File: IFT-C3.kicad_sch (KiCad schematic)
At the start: 47 parts, among them IC1 DIO5508XS8, J1 Conn_01x04_Socket, J2 Conn_01x10_Pin, J3 USB4085-GF-A_REVB, J4 Conn_01x10_Pin, J5 SJ-3523-SMT-TR, J6 Conn_01x02_Pin, J7 Conn_01x02, Q12 Q_Photo_NPN, Q2 Q_NMOS_GSD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

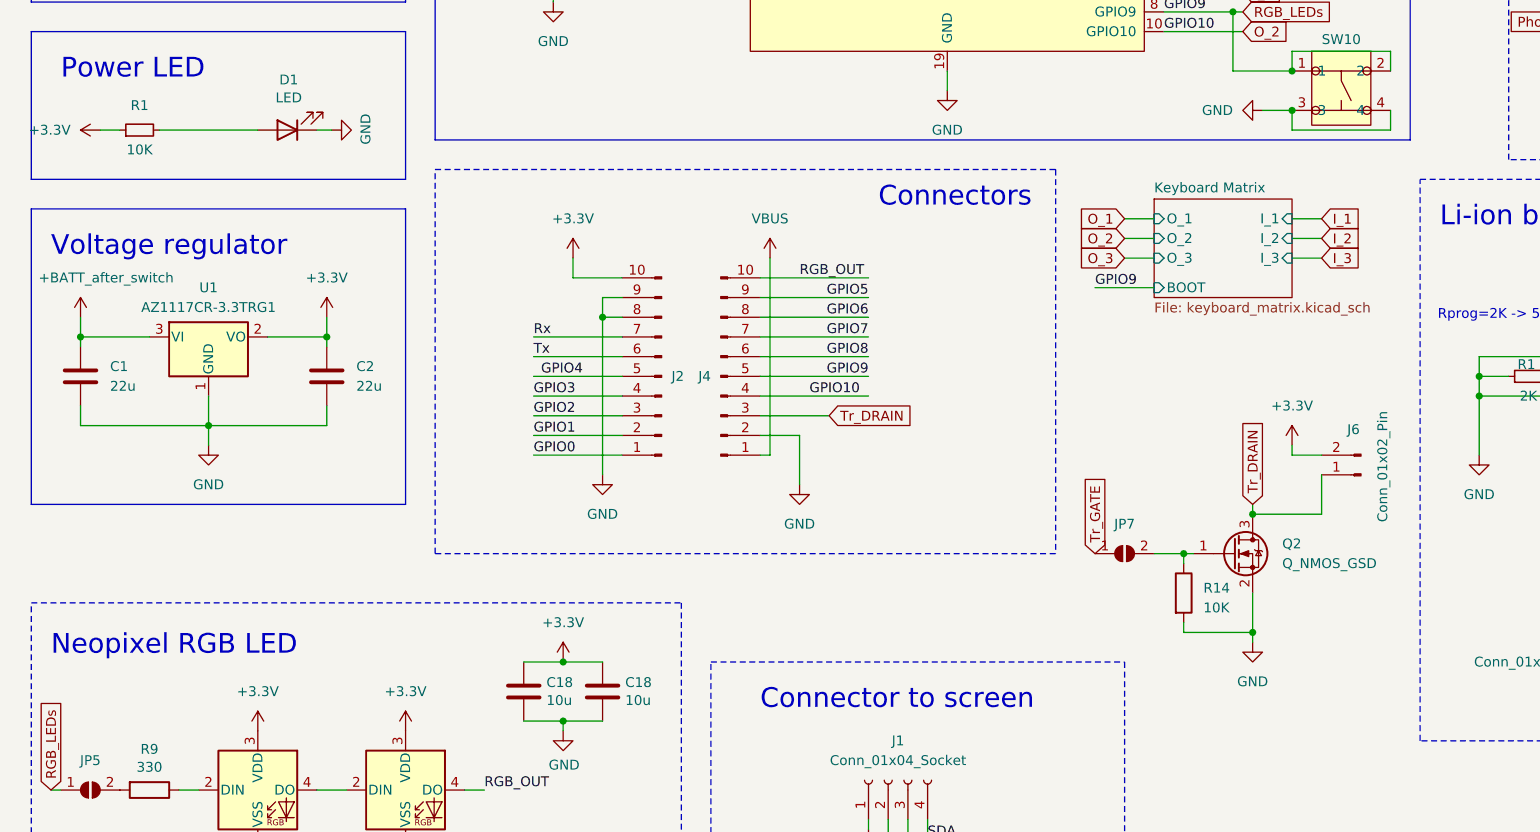
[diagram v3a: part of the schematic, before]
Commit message: Buttons fixed, boot buuton added, footprint of the switch should be easier to solder by hand
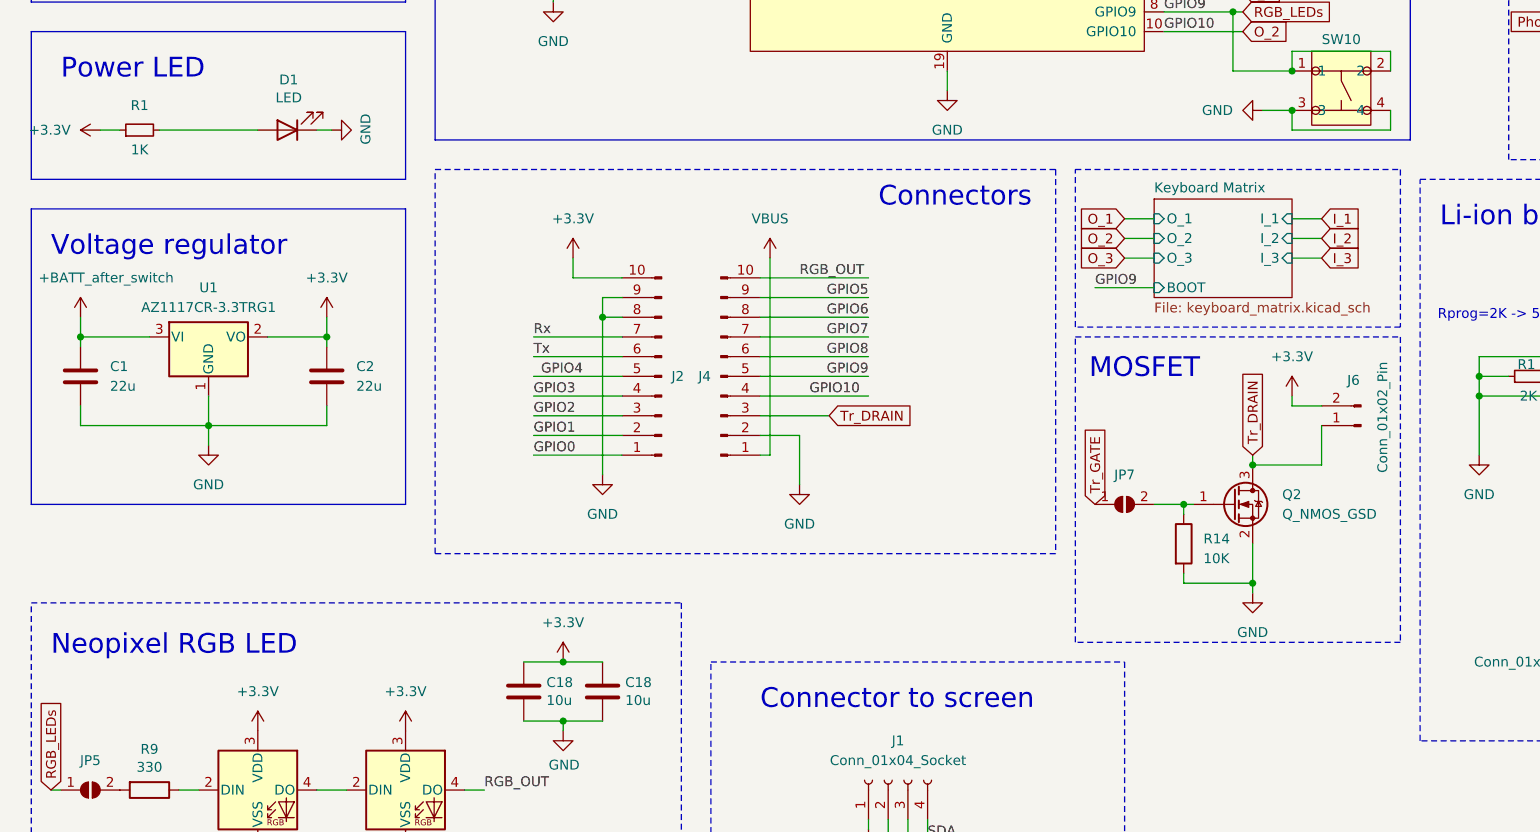
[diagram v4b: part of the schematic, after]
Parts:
- J2, J4: footprint Connector_PinHeader_2.54mm:PinHeader_1x10_P2.54mm_Horizontal -> Connector_PinHeader_2.54mm:PinHeader_1x10_P2.54mm_Vertical
- R1: value 10K -> 1K
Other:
- note added: "MOSFET"
- moved on the sheet: J6, JP7, Q2, R14
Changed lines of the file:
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@@
 	)
 	(junction
-		(at 173.99 149.86)
+		(at 173.99 143.51)
 		(diameter 0)
 		(color 0 0 0 0)
@@
 	)
 	(junction
-		(at 173.99 134.62)
+		(at 173.99 128.27)
 		(diameter 0)
 		(color 0 0 0 0)
@@
 	)
 	(junction
-		(at 165.1 139.7)
+		(at 165.1 133.35)
 		(diameter 0)
 		(color 0 0 0 0)
@@
 	(wire
 		(pts
-			(xy 165.1 148.59) (xy 165.1 149.86)
+			(xy 165.1 142.24) (xy 165.1 143.51)
 		)
 		(stroke
@@
 	(wire
 		(pts
-			(xy 166.37 139.7) (xy 165.1 139.7)
+			(xy 166.37 133.35) (xy 165.1 133.35)
 		)
 		(stroke
@@
 	(wire
 		(pts
-			(xy 165.1 149.86) (xy 173.99 149.86)
+			(xy 165.1 143.51) (xy 173.99 143.51)
 		)
 		(stroke
@@
 	(wire
 		(pts
-			(xy 182.88 129.54) (xy 182.88 134.62)
+			(xy 182.88 123.19) (xy 182.88 128.27)
 		)
 		(stroke
@@
 	(wire
 		(pts
-			(xy 182.88 134.62) (xy 173.99 134.62)
+			(xy 182.88 128.27) (xy 173.99 128.27)
 		)
 		(stroke
@@
 	(wire
 		(pts
-			(xy 173.99 149.86) (xy 173.99 151.13)
+			(xy 173.99 143.51) (xy 173.99 144.78)
 		)
 		(stroke
@@
 	(wire
 		(pts
-			(xy 173.99 144.78) (xy 173.99 149.86)
+			(xy 173.99 138.43) (xy 173.99 143.51)
 		)
 		(stroke
@@
 	(wire
 		(pts
-			(xy 182.88 127) (xy 179.07 127)
+			(xy 182.88 120.65) (xy 179.07 120.65)
 		)
 		(stroke
@@
 	(wire
 		(pts
-			(xy 179.07 127) (xy 179.07 125.73)
+			(xy 179.07 120.65) (xy 179.07 119.38)
 		)
 		(stroke
@@
 	(wire
 		(pts
-			(xy 173.99 133.35) (xy 173.99 134.62)
+			(xy 173.99 127) (xy 173.99 128.27)
 		)
 		(stroke
@@
 	(wire
 		(pts
-			(xy 165.1 139.7) (xy 165.1 140.97)
+			(xy 165.1 133.35) (xy 165.1 134.62)
 		)
 		(stroke
@@
 	(wire
 		(pts
-			(xy 161.29 139.7) (xy 165.1 139.7)
+			(xy 161.29 133.35) (xy 165.1 133.35)
 		)
 		(stroke
@@
 	)
 	(rectangle
+		(start 151.13 90.17)
+		(end 193.04 110.49)
+		(stroke
+			(width 0)
+			(type dash)
+		)
+		(fill
+			(type none)
+		)
+	)
+	(rectangle
 		(start 195.58 91.44)
 		(end 281.94 163.83)
@@
 	)
 	(rectangle
+		(start 151.13 111.76)
+		(end 193.04 151.13)
+		(stroke
+			(width 0)
+			(type dash)
+		)
+		(fill
+			(type none)
+		)
+	)
+	(rectangle
 		(start 250.19 52.07)
 		(end 281.94 88.9)
@@
 		)
 	)
+	(text "MOSFET"
+		(exclude_from_sim no)
+		(at 152.908 117.348 0)
+		(effects
+			(font
+				(size 2.54 2.54)
+			)
+			(justify left bottom)
+		)
+	)
 	(text "Audio output"
 		(exclude_from_sim no)
@@
 	(global_label "Tr_GATE"
 		(shape input)
-		(at 153.67 139.7 90)
+		(at 153.67 133.35 90)
 		(fields_autoplaced yes)
 		(effects
@@
 		)
 		(property "Intersheetrefs" "${INTERSHEET_REFS}"
-			(at 153.67 130.1724 90)
+			(at 153.67 123.8224 90)
 			(effects
 				(font
@@
 	(global_label "Tr_DRAIN"
 		(shape input)
-		(at 173.99 133.35 90)
+		(at 173.99 127 90)
 		(fields_autoplaced yes)
 		(effects
@@
 		)
 		(property "Intersheetrefs" "${INTERSHEET_REFS}"
-			(at 173.99 122.7337 90)
+			(at 173.99 116.3837 90)
 			(effects
 				(font
@@
 	(symbol
 		(lib_id "Device:Q_NMOS_GSD")
-		(at 171.45 139.7 0)
+		(at 171.45 133.35 0)
 		(unit 1)
 		(exclude_from_sim no)
@@
 		(fields_autoplaced yes)
 		(property "Reference" "Q2"
-			(at 177.8 138.43 0)
+			(at 177.8 132.08 0)
 			(effects
 				(font
@@
 		)
 		(property "Value" "Q_NMOS_GSD"
-			(at 177.8 140.97 0)
+			(at 177.8 134.62 0)
 			(effects
 				(font
@@
 		)
 		(property "Footprint" "Package_TO_SOT_SMD:SOT-23-3"
-			(at 176.53 137.16 0)
+			(at 176.53 130.81 0)
 			(effects
 				(font
@@
 		)
 		(property "Datasheet" "~"
-			(at 171.45 139.7 0)
+			(at 171.45 133.35 0)
 			(effects
 				(font
@@
 		)
 		(property "Description" ""
-			(at 171.45 139.7 0)
+			(at 171.45 133.35 0)
 			(effects
 				(font
@@
 			)
 		)
-		(property "Value" "10K"
+		(property "Value" "1K"
 			(at 30.48 87.63 90)
 			(effects
@@
 			)
 		)
-		(property "Footprint" "Connector_PinHeader_2.54mm:PinHeader_1x10_P2.54mm_Horizontal"
+		(property "Footprint" "Connector_PinHeader_2.54mm:PinHeader_1x10_P2.54mm_Vertical"
 			(at 97.79 116.84 0)
 			(effects
@@
 	(symbol
 		(lib_id "power:+3.3V")
-		(at 179.07 125.73 0)
+		(at 179.07 119.38 0)
 		(unit 1)
 		(exclude_from_sim no)
@@
 		(fields_autoplaced yes)
 		(property "Reference" "#PWR049"
-			(at 179.07 129.54 0)
+			(at 179.07 123.19 0)
 			(effects
 				(font
@@
 		)
 		(property "Value" "+3.3V"
-			(at 179.07 120.65 0)
+			(at 179.07 114.3 0)
 			(effects
 				(font
@@
 		)
 		(property "Footprint" ""
-			(at 179.07 125.73 0)
+			(at 179.07 119.38 0)
 			(effects
 				(font
@@
 		)
 		(property "Datasheet" ""
-			(at 179.07 125.73 0)
+			(at 179.07 119.38 0)
 			(effects
 				(font
@@
 		)
 		(property "Description" ""
-			(at 179.07 125.73 0)
+			(at 179.07 119.38 0)
 			(effects
 				(font
@@
 			)
 		)
-		(property "Footprint" "Connector_PinHeader_2.54mm:PinHeader_1x10_P2.54mm_Horizontal"
+		(property "Footprint" "Connector_PinHeader_2.54mm:PinHeader_1x10_P2.54mm_Vertical"
 			(at 105.41 116.84 0)
 			(effects
@@
 	(symbol
 		(lib_id "Connector:Conn_01x02_Pin")
-		(at 187.96 129.54 180)
+		(at 187.96 123.19 180)
 		(unit 1)
 		(exclude_from_sim no)
@@
 		(dnp no)
 		(property "Reference" "J6"
-			(at 186.182 123.698 0)
+			(at 186.182 117.348 0)
 			(effects
 				(font
@@
 		)
 		(property "Value" "Conn_01x02_Pin"
-			(at 190.754 135.636 90)
+			(at 190.754 129.286 90)
 			(effects
 				(font
@@
 		)
 		(property "Footprint" "Motors:Vybronics_VZ30C1T8219732L"
-			(at 187.96 129.54 0)
+			(at 187.96 123.19 0)
 			(effects
 				(font
@@
 		)
 		(property "Datasheet" "~"
-			(at 187.96 129.54 0)
+			(at 187.96 123.19 0)
 			(effects
 				(font
@@
 		)
 		(property "Description" "Generic connector, single row, 01x02, script generated"
-			(at 187.96 129.54 0)
+			(at 187.96 123.19 0)
 			(effects
 				(font
@@
 	(symbol
 		(lib_id "Device:R")
-		(at 165.1 144.78 0)
+		(at 165.1 138.43 0)
 		(unit 1)
 		(exclude_from_sim no)
@@
 		(fields_autoplaced yes)
 		(property "Reference" "R14"
-			(at 167.64 144.145 0)
+			(at 167.64 137.795 0)
 			(effects
 				(font
@@
 		)
 		(property "Value" "10K"
-			(at 167.64 146.685 0)
+			(at 167.64 140.335 0)
 			(effects
 				(font
@@
 		)
 		(property "Footprint" "Resistor_SMD:R_0805_2012Metric_Pad1.20x1.40mm_HandSolder"
-			(at 163.322 144.78 90)
+			(at 163.322 138.43 90)
 			(effects
 				(font
@@
 		)
 		(property "Datasheet" "~"
-			(at 165.1 144.78 0)
+			(at 165.1 138.43 0)
 			(effects
 				(font
@@
 		)
 		(property "Description" ""
-			(at 165.1 144.78 0)
+			(at 165.1 138.43 0)
 			(effects
 				(font
@@
 	(symbol
 		(lib_id "power:GND")
-		(at 173.99 151.13 0)
+		(at 173.99 144.78 0)
 		(unit 1)
 		(exclude_from_sim no)
@@
 		(fields_autoplaced yes)
 		(property "Reference" "#PWR048"
-			(at 173.99 157.48 0)
+			(at 173.99 151.13 0)
 			(effects
 				(font
@@
 		)
 		(property "Value" "GND"
-			(at 173.99 156.21 0)
+			(at 173.99 149.86 0)
 			(effects
 				(font
@@
 		)
 		(property "Footprint" ""
-			(at 173.99 151.13 0)
+			(at 173.99 144.78 0)
 			(effects
 				(font
@@
 		)
 		(property "Datasheet" ""
-			(at 173.99 151.13 0)
+			(at 173.99 144.78 0)
 			(effects
 				(font
@@
 		)
 		(property "Description" ""
-			(at 173.99 151.13 0)
+			(at 173.99 144.78 0)
 			(effects
 				(font
@@
 	(symbol
 		(lib_id "Jumper:SolderJumper_2_Open")
-		(at 157.48 139.7 0)
+		(at 157.48 133.35 0)
 		(unit 1)
 		(exclude_from_sim no)
@@
 		(fields_autoplaced yes)
 		(property "Reference" "JP7"
-			(at 157.48 135.89 0)
+			(at 157.48 129.54 0)
 			(effects
 				(font
@@
 		)
 		(property "Value" "SolderJumper_2_Open"
-			(at 157.48 135.89 0)
+			(at 157.48 129.54 0)
 			(effects
 				(font
@@
 		)
 		(property "Footprint" "Jumper:SolderJumper-2_P1.3mm_Open_TrianglePad1.0x1.5mm"
-			(at 157.48 139.7 0)
+			(at 157.48 133.35 0)
 			(effects
 				(font
@@
 		)
 		(property "Datasheet" "~"
-			(at 157.48 139.7 0)
+			(at 157.48 133.35 0)
 			(effects
 				(font
@@
 		)
 		(property "Description" ""
-			(at 157.48 139.7 0)
+			(at 157.48 133.35 0)
 			(effects
 				(font
